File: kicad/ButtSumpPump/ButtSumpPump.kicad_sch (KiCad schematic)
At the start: 10 parts, among them J1 Butt Freq Sensor, J10 Screw_Terminal_01x03, J2 Sump Freq Sensor, J3 Conn_01x03_Pin, J4 Conn_01x03_Pin, J5 ESP32-WROOM-32, J6 12v DC, J7 Screw_Terminal_01x03, J8 Screw_Terminal_01x03, J9 Screw_Terminal_01x03

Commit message: Updates to drawing
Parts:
- added U1: ~, symbol ESP32:ESP32-WROOM-DEV-MODULE
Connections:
- new net Butt Sensor Input: U1.8 (D25)
- new net Pump Relay Output: U1.19 (D2)
- new net Sump Sensor Input: U1.7 (D33)
- new net Valve Relay Output: U1.20 (D4)
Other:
- moved on the sheet: J6
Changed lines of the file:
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@@
 	(label "D4 output - Valve Relay Pin"
 		(at 38.1 125.73 0)
+		(fields_autoplaced yes)
 		(effects
 			(font
@@
 	(label "Vin (5v)"
 		(at 38.1 113.03 0)
+		(fields_autoplaced yes)
 		(effects
 			(font
@@
 	(label "GND(EN)"
 		(at 38.1 115.57 0)
-		(effects
-			(font
-				(size 1.27 1.27)
-			)
-			(justify left bottom)
+		(fields_autoplaced yes)
+		(effects
+			(font
+				(size 1.27 1.27)
+			)
+			(justify left bottom)
+		)
+	)
+	(label "Butt Sensor Input"
+		(at 85.09 161.29 180)
+		(effects
+			(font
+				(size 1.27 1.27)
+			)
+			(justify right bottom)
 		)
 	)
@@
 	(label "GND"
 		(at 163.83 20.32 180)
+		(fields_autoplaced yes)
 		(effects
 			(font
@@
 			)
 			(justify right bottom)
+		)
+	)
+	(label "Valve Relay Output"
+		(at 106.68 168.91 0)
+		(effects
+			(font
+				(size 1.27 1.27)
+			)
+			(justify left bottom)
 		)
 	)
 	(label "3v3"
 		(at 163.83 22.86 180)
+		(fields_autoplaced yes)
 		(effects
 			(font
@@
 	(label "D33 input - Sump Sensor Pin"
 		(at 38.1 120.65 0)
+		(fields_autoplaced yes)
 		(effects
 			(font
@@
 	(label "Pin_9"
 		(at 38.1 130.81 0)
+		(fields_autoplaced yes)
 		(effects
 			(font
@@
 	(label "Pin_11"
 		(at 38.1 135.89 0)
+		(fields_autoplaced yes)
 		(effects
 			(font
@@
 	(label "GND(BOOT)"
 		(at 38.1 118.11 0)
+		(fields_autoplaced yes)
 		(effects
 			(font
@@
 	(label "Hz"
 		(at 163.83 25.4 180)
+		(fields_autoplaced yes)
 		(effects
 			(font
@@
 	(label "GND"
 		(at 198.12 20.32 0)
+		(fields_autoplaced yes)
 		(effects
 			(font
@@
 	(label "3v3"
 		(at 38.1 110.49 0)
+		(fields_autoplaced yes)
 		(effects
 			(font
@@
 	(label "Pin_10"
 		(at 38.1 133.35 0)
+		(fields_autoplaced yes)
 		(effects
 			(font
@@
 	(label "3v3"
 		(at 198.12 22.86 0)
+		(fields_autoplaced yes)
 		(effects
 			(font
@@
 	(label "D2 output - Pump Relay Pin"
 		(at 38.1 128.27 0)
+		(fields_autoplaced yes)
 		(effects
 			(font
@@
 	(label "Hz"
 		(at 198.12 25.4 0)
-		(effects
-			(font
-				(size 1.27 1.27)
-			)
-			(justify left bottom)
+		(fields_autoplaced yes)
+		(effects
+			(font
+				(size 1.27 1.27)
+			)
+			(justify left bottom)
+		)
+	)
+	(label "Sump Sensor Input"
+		(at 85.09 158.75 180)
+		(effects
+			(font
+				(size 1.27 1.27)
+			)
+			(justify right bottom)
 		)
 	)
 	(label "D25 input - Butt Sensor Pin"
 		(at 38.1 123.19 0)
+		(fields_autoplaced yes)
+		(effects
+			(font
+				(size 1.27 1.27)
+			)
+			(justify left bottom)
+		)
+	)
+	(label "Pump Relay Output"
+		(at 106.68 171.45 0)
 		(effects
 			(font
@@
 	)
 	(symbol
+		(lib_id "ESP32:ESP32-WROOM-DEV-MODULE")
+		(at 106.68 146.05 0)
+		(unit 1)
+		(exclude_from_sim no)
+		(in_bom yes)
+		(on_board yes)
+		(dnp no)
+		(fields_autoplaced yes)
+		(property "Reference" "U1"
+			(at 95.885 138.43 0)
+			(effects
+				(font
+					(size 1.27 1.27)
+				)
+			)
+		)
+		(property "Value" "~"
+			(at 95.885 140.97 0)
+			(effects
+				(font
+					(size 1.27 1.27)
+				)
+			)
+		)
+		(property "Footprint" ""
+			(at 87.63 146.05 0)
+			(effects
+				(font
+					(size 1.27 1.27)
+				)
+				(hide yes)
+			)
+		)
+		(property "Datasheet" ""
+			(at 87.63 146.05 0)
+			(effects
+				(font
+					(size 1.27 1.27)
+				)
+				(hide yes)
+			)
+		)
+		(property "Description" ""
+			(at 87.63 146.05 0)
+			(effects
+				(font
+					(size 1.27 1.27)
+				)
+				(hide yes)
+			)
+		)
+		(pin "15"
+		)
+		(pin "19"
+		)
+		(pin "14"
+		)
+		(pin "13"
+		)
+		(pin "18"
+		)
+		(pin "11"
+		)
+		(pin "12"
+		)
+		(pin "16"
+		)
+		(pin "10"
+		)
+		(pin "1"
+		)
+		(pin "17"
+		)
+		(pin "20"
+		)
+		(pin "22"
+		)
+		(pin "21"
+		)
+		(pin "23"
+		)
+		(pin "24"
+		)
+		(pin "25"
+		)
+		(pin "2"
+		)
+		(pin "26"
+		)
+		(pin "27"
+		)
+		(pin "28"
+		)
+		(pin "29"
+		)
+		(pin "3"
+		)
+		(pin "30"
+		)
+		(pin "4"
+		)
+		(pin "5"
+		)
+		(pin "9"
+		)
+		(pin "7"
+		)
+		(pin "8"
+		)
+		(pin "6"
+		)
+		(instances
+			(project ""
+				(path "/34303405-45fc-4e24-b294-439bbbab4fcb"
+					(reference "U1")
+					(unit 1)
+				)
+			)
+		)
+	)
+	(symbol
 		(lib_id "Connector:Conn_01x03_Pin")
 		(at 205.74 39.37 0)
@@
 	(symbol
 		(lib_id "Connector:Screw_Terminal_01x02")
-		(at 26.67 31.75 0)
+		(at 140.97 140.97 0)
 		(mirror y)
 		(unit 1)
@@
 		(fields_autoplaced yes)
 		(property "Reference" "J6"
-			(at 26.67 25.4 0)
+			(at 140.97 134.62 0)
 			(effects
 				(font
@@
 		)
 		(property "Value" "12v DC"
-			(at 26.67 27.94 0)
+			(at 140.97 137.16 0)
 			(effects
 				(font
@@
 		)
 		(property "Footprint" ""
-			(at 26.67 31.75 0)
+			(at 140.97 140.97 0)
 			(effects
 				(font
@@
 		)
 		(property "Datasheet" "~"
-			(at 26.67 31.75 0)
+			(at 140.97 140.97 0)
 			(effects
 				(font
@@
 		)
 		(property "Description" "Generic screw terminal, single row, 01x02, script generated (kicad-library-utils/schlib/autogen/connector/)"
-			(at 26.67 31.75 0)
-			(effects
-				(font
+			(at 140.97 140.97 0)
+			(effects
+				(font

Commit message: update to drawing
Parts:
- removed J10, J7, J8, J9: Screw_Terminal_01x03, symbol Connector:Screw_Terminal_01x03
- removed J3, J4: Conn_01x03_Pin, symbol Connector:Conn_01x03_Pin
- removed J5: ESP32-WROOM-32, symbol Connector:Conn_01x30_Pin
- added U2: ~, symbol 12v pump:12v_pump
- added U2-VALVE1, U3-PUMP: ~, symbol PSU:Relay
- added U3: ~, symbol 12v pump:12v Ball Valve
- added U4-12v-5v: ~, symbol PSU:12v-5v
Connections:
- net Sump Sensor Input is gone; now on net D33: U1.7 (D33)
- net 12v: now also J6.1 (Pin_1), U2-VALVE1.6 (12v), U3-PUMP.2 (COM), U3-PUMP.6 (12v), U4-12v-5v.1 (12v)
- net 3v3: now also U1.16 (3v3)
- net GND: now also J6.2 (Pin_2), U2-VALVE1.5 (GND), U2.2 (GND), U3-PUMP.5 (GND), U3.2 (YELLOW_GND), U4-12v-5v.2 (GND)
- net at U1.14 (GND): now also U4-12v-5v.4 (GND)
- net at U1.15 (VIN): now also U4-12v-5v.3 (5v)
- net Butt Sensor Input renamed D25
- net D25: now also J1.3 (Pin_3)
- net Hz renamed D33
- net D33: no longer J1.3 (Pin_3)
- net Pump Relay Output renamed D2
- net D2: now also U3-PUMP.4 (EN_3v3)
- net Valve Relay Output renamed D4
- net D4: now also U2-VALVE1.4 (EN_3v3)
- new net: U2.1 (12v), U3-PUMP.1 (NO)
- new net: U2-VALVE1.1 (NO), U3.1 (12V_RED_OPEN)
- new net: U2-VALVE1.3 (NC), U3.3 (12V_BLUE_CLOSE)
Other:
- note removed: "RELAY"
- moved on the sheet: J1, J6, U1

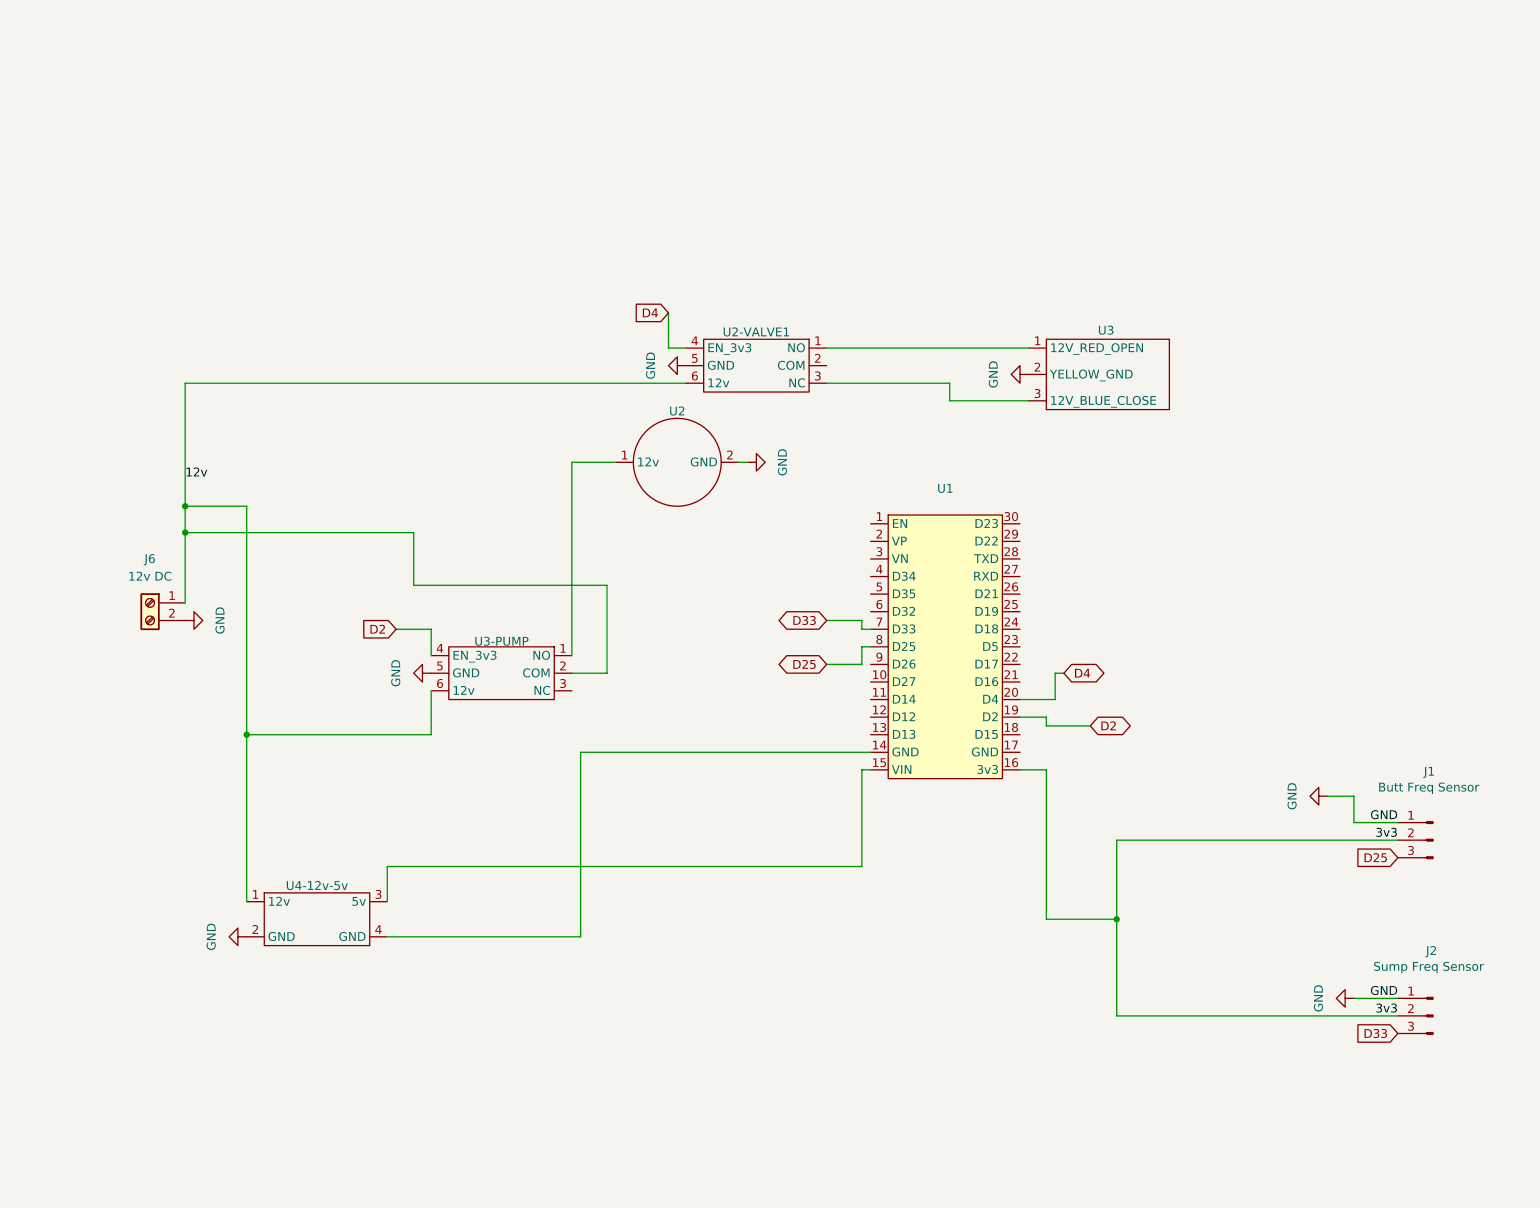
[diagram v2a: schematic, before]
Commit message: Identified locations of circuitry on wiring diagram
Also made PSU 12v component
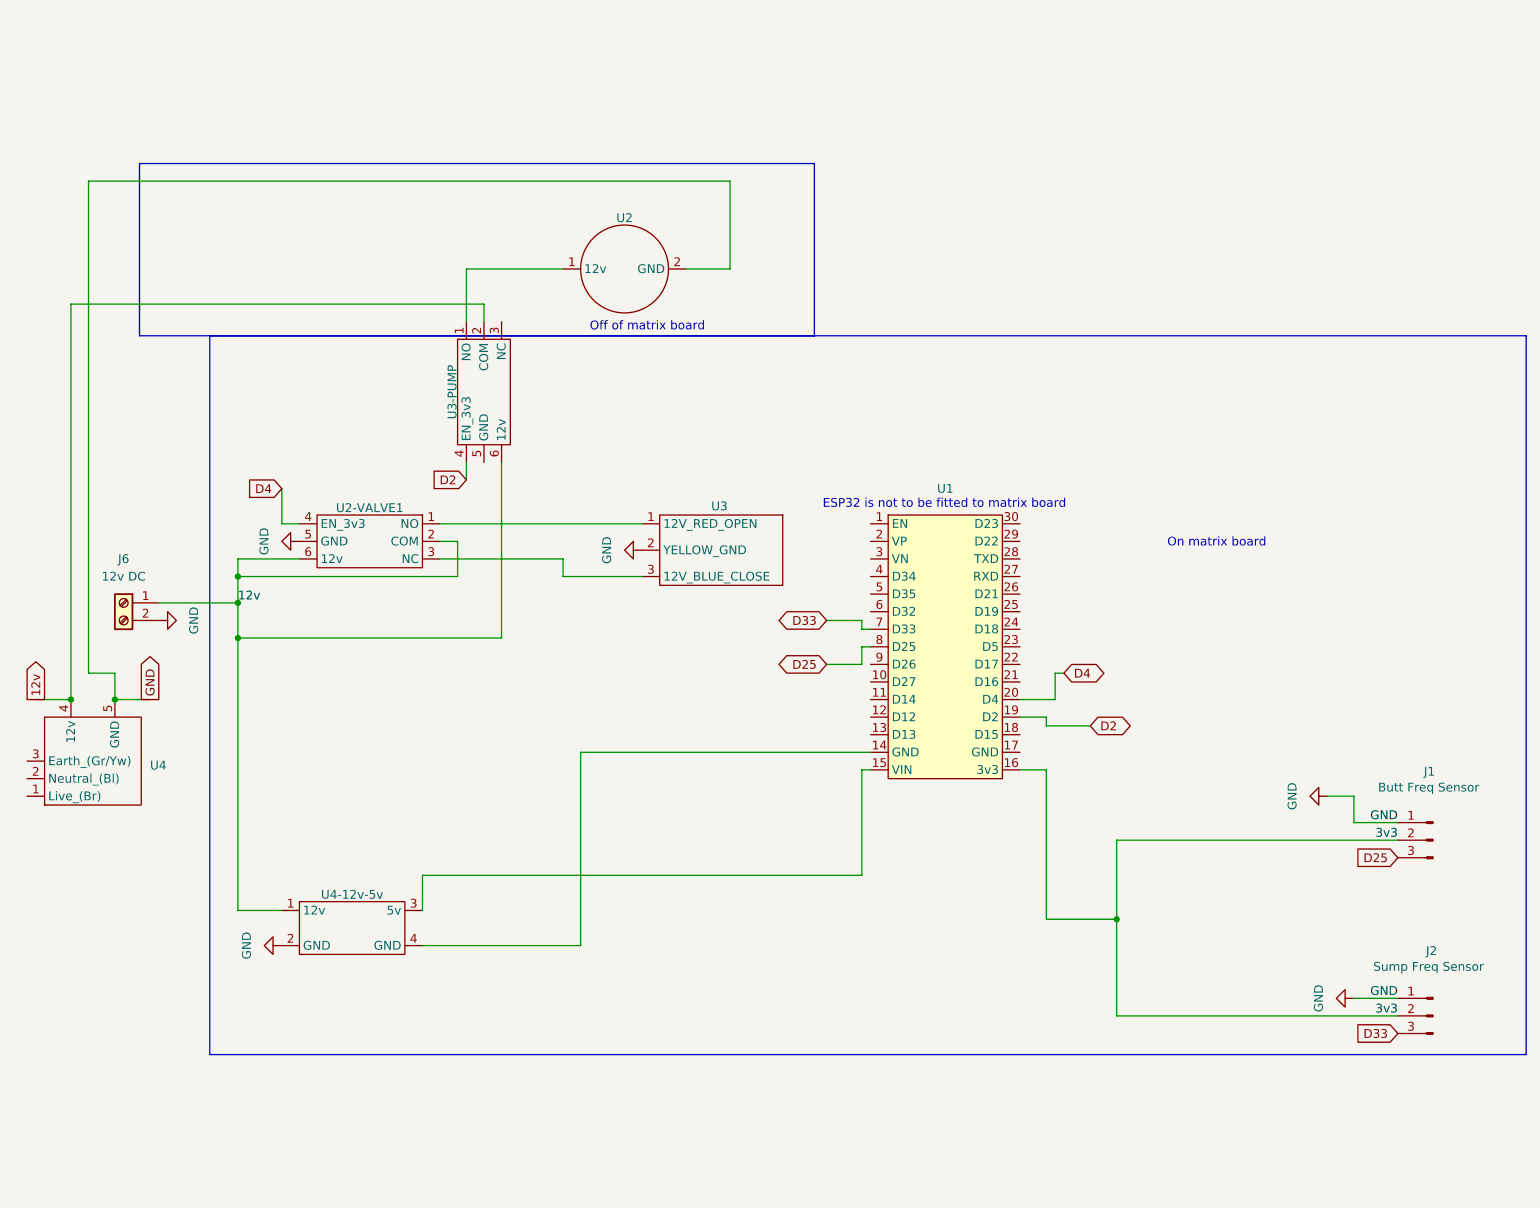
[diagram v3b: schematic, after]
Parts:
- added U4: ~, symbol PSU:12v_PSU
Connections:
- net 12v: now also U2-VALVE1.2 (COM), U4.4 (12v)
- net GND: now also U4.5 (GND); no longer U3-PUMP.5 (GND)
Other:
- note added: "ESP32 is not to be fitted to matrix board"
- note added: "Off of matrix board"
- note added: "On matrix board"
- moved on the sheet: J6, U2, U2-VALVE1, U3, U3-PUMP, U4-12v-5v

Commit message: Added nPCV and fPOV functions for turning on and off the relays.
Also added further updates to drawings.

Code now keeps valve open if there is not enough to trigger the sensor level trip.
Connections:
- net GND: now also U1.17 (GND)
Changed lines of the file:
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@@
+	)
+	(junction
+		(at 191.77 127)
+		(diameter 0)
+		(color 0 0 0 0)
 	)
 	(junction
@@
 	(wire
 		(pts
+			(xy 191.77 127) (xy 205.74 127)
+		)
+		(stroke
+			(width 0)
+			(type default)
+		)
+	)
+	(wire
+		(pts
 			(xy 50.8 87.63) (xy 53.34 87.63)
 		)
@@
 	(wire
 		(pts
+			(xy 191.77 127) (xy 191.77 156.21)
+		)
+		(stroke
+			(width 0)
+			(type default)
+		)
+	)
+	(wire
+		(pts
 			(xy 134.62 107.95) (xy 134.62 105.41)
 		)
@@
 	(wire
 		(pts
-			(xy 205.74 156.21) (xy 212.09 156.21)
+			(xy 170.18 127) (xy 191.77 127)
+		)
+		(stroke
+			(width 0)
+			(type default)
+		)
+	)
+	(wire
+		(pts
+			(xy 170.18 127) (xy 170.18 120.65)
 		)
 		(stroke
@@
 	(wire
 		(pts
+			(xy 157.48 120.65) (xy 170.18 120.65)
+		)
+		(stroke
+			(width 0)
+			(type default)
+		)
+	)
+	(wire
+		(pts
 			(xy 161.29 123.19) (xy 161.29 144.78)
 		)
@@
 	(wire
 		(pts
-			(xy 201.93 127) (xy 205.74 127)
+			(xy 191.77 156.21) (xy 212.09 156.21)
 		)
 		(stroke
@@
 				(path "/34303405-45fc-4e24-b294-439bbbab4fcb"
 					(reference "U1")
-					(unit 1)
-				)
-			)
-		)
-	)
-	(symbol
-		(lib_id "power:GND")
-		(at 201.93 127 270)
-		(unit 1)
-		(exclude_from_sim no)
-		(in_bom yes)
-		(on_board yes)
-		(dnp no)
-		(fields_autoplaced yes)
-		(property "Reference" "#PWR02"
-			(at 195.58 127 0)
-			(effects
-				(font
-					(size 1.27 1.27)
-				)
-				(hide yes)
-			)
-		)
-		(property "Value" "GND"
-			(at 196.85 127 0)
-			(effects
-				(font
-					(size 1.27 1.27)
-				)
-			)
-		)
-		(property "Footprint" ""
-			(at 201.93 127 0)
-			(effects
-				(font
-					(size 1.27 1.27)
-				)
-				(hide yes)
-			)
-		)
-		(property "Datasheet" ""
-			(at 201.93 127 0)
-			(effects
-				(font
-					(size 1.27 1.27)
-				)
-				(hide yes)
-			)
-		)
-		(property "Description" "Power symbol creates a global label with name \"GND\" , ground"
-			(at 201.93 127 0)
-			(effects
-				(font
-					(size 1.27 1.27)
-				)
-				(hide yes)
-			)
-		)
-		(pin "1"
-		)
-		(instances
-			(project "ButtSumpPump"
-				(path "/34303405-45fc-4e24-b294-439bbbab4fcb"
-					(reference "#PWR02")
 					(unit 1)
 				)
@@
 					(unit 1)
 				)
-			)
-		)
-	)
-	(symbol
-		(lib_id "power:GND")
-		(at 205.74 156.21 270)
-		(unit 1)
-		(exclude_from_sim no)
-		(in_bom yes)
-		(on_board yes)
-		(dnp no)
-		(fields_autoplaced yes)
-		(property "Reference" "#PWR03"
-			(at 199.39 156.21 0)
-			(effects
-				(font
-					(size 1.27 1.27)
-				)
-				(hide yes)
-			)
-		)
-		(property "Value" "GND"
-			(at 200.66 156.21 0)
-			(effects
-				(font
-					(size 1.27 1.27)
-				)
-			)
-		)
-		(property "Footprint" ""
-			(at 205.74 156.21 0)
-			(effects
-				(font
-					(size 1.27 1.27)
-				)
-				(hide yes)
-			)
-		)
-		(property "Datasheet" ""
-			(at 205.74 156.21 0)
-			(effects
-				(font
-					(size 1.27 1.27)
-				)
-				(hide yes)
-			)
-		)
-		(property "Description" "Power symbol creates a global label with name \"GND\" , ground"
-			(at 205.74 156.21 0)
-			(effects
-				(font
-					(size 1.27 1.27)
-				)
-				(hide yes)
-			)
-		)
-		(pin "1"
-		)
-		(instances
-			(project "ButtSumpPump"
-				(path "/34303405-45fc-4e24-b294-439bbbab4fcb"
-					(reference "#PWR03")
-					(unit 1)
-				)
